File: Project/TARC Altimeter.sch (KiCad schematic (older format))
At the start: 19 parts, among them J1 Power Switch, J2 Programmer Breakout (Conn_01x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, J3 CS Switch, Q1 Q_NMOS_GSD, U1 A23_Socket, U2 ATtiny85-20SU, U3 AP2210-3.3, U4 BMP280

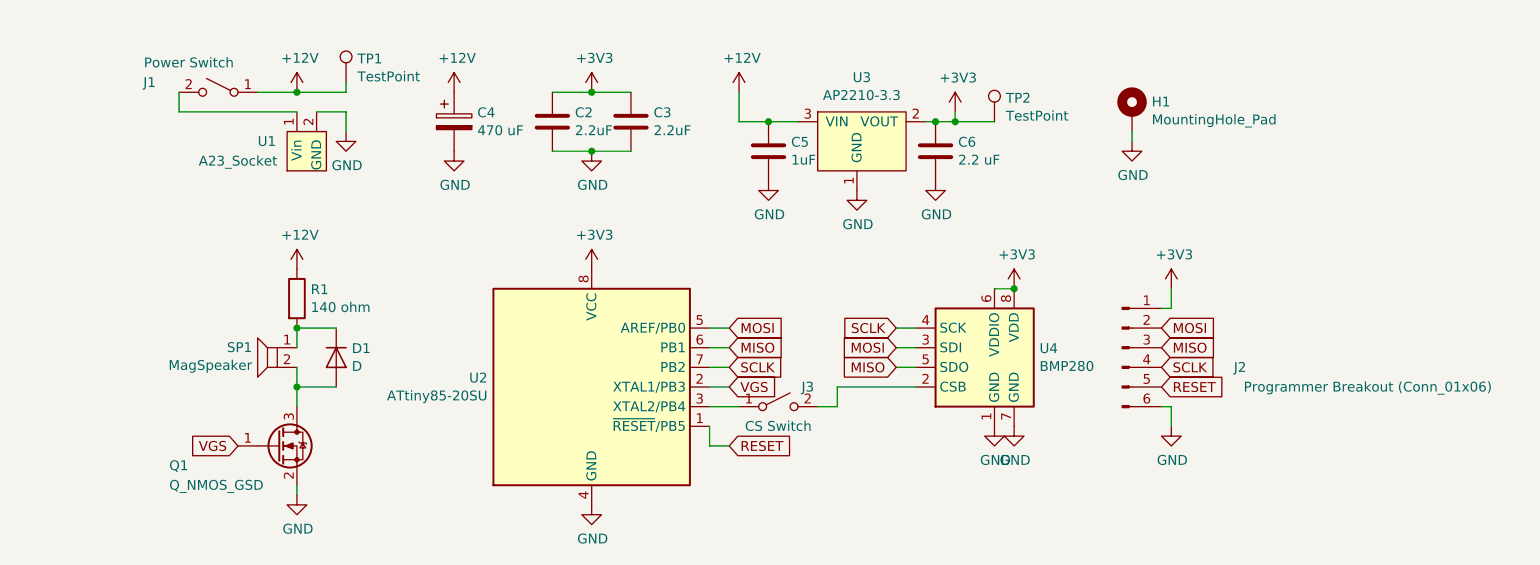
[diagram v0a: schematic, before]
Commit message: added i2c pullups and rearranged components, finalized BMP280 test script
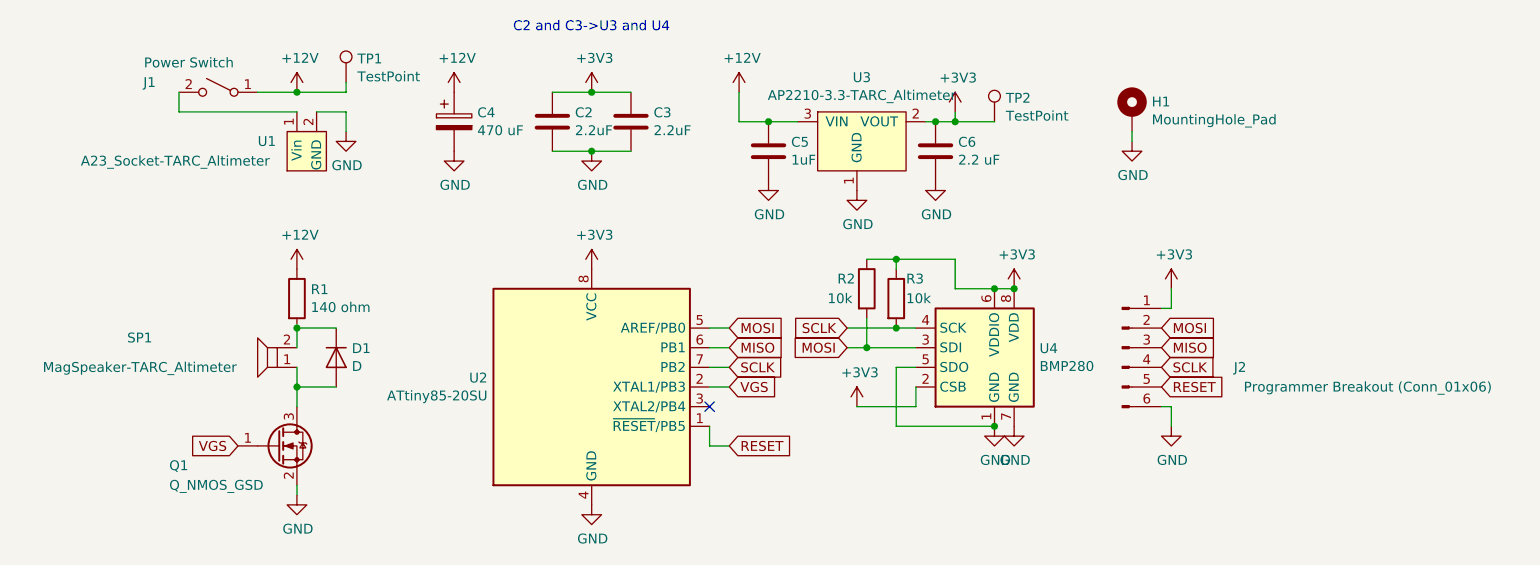
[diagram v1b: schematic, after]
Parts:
- removed J3: CS Switch, Connector_PinHeader_1.27mm:PinHeader_1x02_P1.27mm_Vertical, symbol Switch:SW_SPST
- removed SP1: MagSpeaker, TARC Altimeter:WT-1205, symbol TARC_Altimeter:MagSpeaker
- removed U1: A23_Socket, TARC Altimeter:A23_Socket, symbol TARC_Altimeter:A23_Socket
- removed U3: AP2210-3.3, Package_TO_SOT_SMD:SOT-23, symbol TARC_Altimeter:AP2210-3.3
- added R2, R3: 10k, Resistor_SMD:R_0805_2012Metric_Pad1.15x1.40mm_HandSolder, symbol Device:R
- added SP1: MagSpeaker-TARC_Altimeter, TARC_Altimeter:WT-1205, symbol TARC-Altimeter-rescue:MagSpeaker-TARC_Altimeter
- added U1: A23_Socket-TARC_Altimeter, TARC_Altimeter:A23_Socket, symbol TARC-Altimeter-rescue:A23_Socket-TARC_Altimeter
- added U3: AP2210-3.3-TARC_Altimeter, Package_TO_SOT_SMD:SOT-23, symbol TARC-Altimeter-rescue:AP2210-3.3-TARC_Altimeter
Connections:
- net +12V: now also U3.3 (VIN)
- net +3V3: now also U4.2 (CSB), R2.1, R3.1, U3.2 (VOUT)
- net GND: now also U4.5 (SDO), U1.2 (GND), U3.1 (GND)
- net MISO: no longer U4.5 (SDO)
- net MOSI: now also R2.2
- net SCLK: now also R3.2
- net at D1.1 (K), R1.2: now also SP1.2
- net at D1.2 (A), Q1.3 (D): now also SP1.1
- net at J1.2 (B): now also U1.1 (Vin)
- no-connect marks 0 -> 1
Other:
- note added: "C2 and C3->U3 and U4"
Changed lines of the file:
@@
 EESchema Schematic File Version 4
-LIBS:TARC Altimeter-cache
-EELAYER 26 0
+EELAYER 30 0
 EELAYER END
 $Descr A4 11693 8268
@@
 	1    0    0    -1
 $EndComp
-$Comp
-L TARC_Altimeter:MagSpeaker SP1
-U 1 1 5CB29159
-P 3450 5350
-F 0 "SP1" H 3178 5551 50  0000 L CNN
-F 1 "MagSpeaker" H 3178 5460 50  0000 L CNN
-F 2 "TARC Altimeter:WT-1205" H 3250 5500 50  0001 C CNN
-F 3 "" H 3250 5500 50  0001 C CNN
-	1    3450 5350
-	-1   0    0    -1
-$EndComp
 Wire Wire Line
 	3950 5150 3950 5050
@@
 $EndComp
 $Comp
-L TARC_Altimeter:AP2210-3.3 U3
-U 1 1 5CB5BA2E
-P 6800 4500
-F 0 "U3" H 6825 5225 50  0000 C CNN
-F 1 "AP2210-3.3" H 6825 5134 50  0000 C CNN
-F 2 "Package_TO_SOT_SMD:SOT-23" H 6800 5200 50  0001 C CNN
-F 3 "" H 6800 5200 50  0001 C CNN
-	1    6800 4500
-	1    0    0    -1
-$EndComp
-$Comp
-L power:GND #PWR0107
-U 1 1 5CB5C4BA
-P 6800 4350
-F 0 "#PWR0107" H 6800 4100 50  0001 C CNN
-F 1 "GND" H 6805 4177 50  0000 C CNN
-F 2 "" H 6800 4350 50  0001 C CNN
-F 3 "" H 6800 4350 50  0001 C CNN
-	1    6800 4350
-	1    0    0    -1
-$EndComp
-$Comp
 L power:+3V3 #PWR0108
 U 1 1 5CB5D138
@@
 Wire Wire Line
 	7100 5250 7000 5250
-Wire Wire Line
-	7100 5150 7000 5150
-Text GLabel 7000 5150 0    50   Input ~ 0
-MOSI
-Wire Wire Line
-	7100 5050 7000 5050
 $Comp
 L Device:Q_NMOS_GSD Q1
@@
 VGS
 $Comp
-L TARC_Altimeter:A23_Socket U1
-U 1 1 5CB93965
-P 4000 4150
-F 0 "U1" H 3750 4200 50  0000 L CNN
-F 1 "A23_Socket" H 3450 4100 50  0000 L CNN
-F 2 "TARC Altimeter:A23_Socket" H 4000 4050 50  0001 C CNN
-F 3 "" H 4000 4050 50  0001 C CNN
-	1    4000 4150
-	1    0    0    -1
-$EndComp
-$Comp
 L power:+12V #PWR0111
 U 1 1 5CB94018
@@
 Text GLabel 6150 5050 2    50   Input ~ 0
 MOSI
-Text GLabel 7000 5250 0    50   Input ~ 0
-MISO
 Wire Wire Line
 	6050 5050 6150 5050
@@
 	1    0    0    -1
 $EndComp
-Text GLabel 7000 5050 0    50   Input ~ 0
-SCLK
 Text GLabel 6150 5150 2    50   Input ~ 0
 MISO
@@
 Wire Wire Line
 	3350 3850 3350 3950
-$Comp
-L Switch:SW_SPST J3
-U 1 1 5D45E1A8
-P 6400 5450
-F 0 "J3" H 6550 5550 50  0000 C CNN
-F 1 "CS Switch" H 6400 5350 50  0000 C CNN
-F 2 "Connector_PinHeader_1.27mm:PinHeader_1x02_P1.27mm_Vertical" H 6400 5450 50  0001 C CNN
-F 3 "~" H 6400 5450 50  0001 C CNN
-	1    6400 5450
-	1    0    0    -1
-$EndComp
-Wire Wire Line
-	6050 5450 6200 5450
-Wire Wire Line
-	6700 5350 7100 5350
-Wire Wire Line
-	6700 5350 6700 5450
-Wire Wire Line
-	6700 5450 6600 5450
 Wire Wire Line
 	6050 5550 6050 5650
@@
 Wire Wire Line
 	8200 4050 8200 4100
+$Comp
+L power:GND #PWR0107
+U 1 1 5CB5C4BA
+P 6800 4350
+F 0 "#PWR0107" H 6800 4100 50  0001 C CNN
+F 1 "GND" H 6805 4177 50  0000 C CNN
+F 2 "" H 6800 4350 50  0001 C CNN
+F 3 "" H 6800 4350 50  0001 C CNN
+	1    6800 4350
+	1    0    0    -1
+$EndComp
+Wire Wire Line
+	7000 5250 7000 5550
+Wire Wire Line
+	7000 5550 7500 5550
+Connection ~ 7500 5550
+$Comp
+L TARC-Altimeter-rescue:A23_Socket-TARC_Altimeter U1
+U 1 1 5FED539E
+P 4000 4150
+F 0 "U1" H 3750 4200 50  0000 L CNN
+F 1 "A23_Socket-TARC_Altimeter" H 2850 4100 50  0000 L CNN
+F 2 "TARC_Altimeter:A23_Socket" H 4000 4050 50  0001 C CNN
+F 3 "" H 4000 4050 50  0001 C CNN
+	1    4000 4150
+	1    0    0    -1
+$EndComp
+$Comp
+L TARC-Altimeter-rescue:MagSpeaker-TARC_Altimeter SP1
+U 1 1 5FED5B84
+P 3450 5050
+F 0 "SP1" H 3750 5100 50  0000 C CNN
+F 1 "MagSpeaker-TARC_Altimeter" H 3750 5250 50  0000 C CNN
+F 2 "TARC_Altimeter:WT-1205" H 3250 5200 50  0001 C CNN
+F 3 "" H 3250 5200 50  0001 C CNN
+	1    3450 5050
+	-1   0    0    1
+$EndComp
+NoConn ~ 6050 5450
+$Comp
+L Device:R R3
+U 1 1 5FEE4847
+P 7000 4900
+F 0 "R3" H 7050 5000 50  0000 L CNN
+F 1 "10k" H 7050 4900 50  0000 L CNN
+F 2 "Resistor_SMD:R_0805_2012Metric_Pad1.15x1.40mm_HandSolder" V 6930 4900 50  0001 C CNN
+F 3 "~" H 7000 4900 50  0001 C CNN
+	1    7000 4900
+	1    0    0    -1
+$EndComp
+$Comp
+L Device:R R2
+U 1 1 5FEE3DD7
+P 6850 4850
+F 0 "R2" H 6700 4900 50  0000 L CNN
+F 1 "10k" H 6650 4800 50  0000 L CNN
+F 2 "Resistor_SMD:R_0805_2012Metric_Pad1.15x1.40mm_HandSolder" V 6780 4850 50  0001 C CNN
+F 3 "~" H 6850 4850 50  0001 C CNN
+	1    6850 4850
+	1    0    0    -1
+$EndComp
+Connection ~ 7000 5050
+Wire Wire Line
+	6750 5050 7000 5050
+Wire Wire Line
+	6750 5150 6850 5150
+Wire Wire Line
+	6850 5000 6850 5150
+Connection ~ 6850 5150
+Wire Wire Line
+	7000 4700 7000 4750
+Wire Wire Line
+	7300 4700 7300 4850
+Connection ~ 7000 4700
+Connection ~ 7500 4850
+Wire Wire Line
+	7300 4850 7500 4850
+Wire Wire Line
+	6850 4700 7000 4700
+Text GLabel 6750 5150 0    50   Input ~ 0
+MOSI
+Text GLabel 6750 5050 0    50   Input ~ 0
+SCLK
+Wire Wire Line
+	7000 5050 7100 5050
+Wire Wire Line
+	6850 5150 7100 5150
+Wire Wire Line
+	7000 4700 7300 4700
+$Comp
+L power:+3V3 #PWR0122
+U 1 1 5FEFA896
+P 6800 5450
+F 0 "#PWR0122" H 6800 5300 50  0001 C CNN
+F 1 "+3V3" H 6815 5623 50  0000 C CNN
+F 2 "" H 6800 5450 50  0001 C CNN
+F 3 "" H 6800 5450 50  0001 C CNN
+	1    6800 5450
+	1    0    0    -1
+$EndComp
+Wire Wire Line
+	6800 5450 7100 5450
+Wire Wire Line
+	7100 5450 7100 5350
+Text Notes 5050 3550 0    50   ~ 0
+C2 and C3->U3 and U4
+$Comp
+L TARC-Altimeter-rescue:AP2210-3.3-TARC_Altimeter U3
+U 1 1 5FED6C3E
+P 6800 4500
+F 0 "U3" H 6825 5225 50  0000 C CNN
+F 1 "AP2210-3.3-TARC_Altimeter" H 6825 5134 50  0000 C CNN
+F 2 "Package_TO_SOT_SMD:SOT-23" H 6800 5200 50  0001 C CNN
+F 3 "" H 6800 5200 50  0001 C CNN
+	1    6800 4500
+	1    0    0    -1
+$EndComp
 $EndSCHEMATC

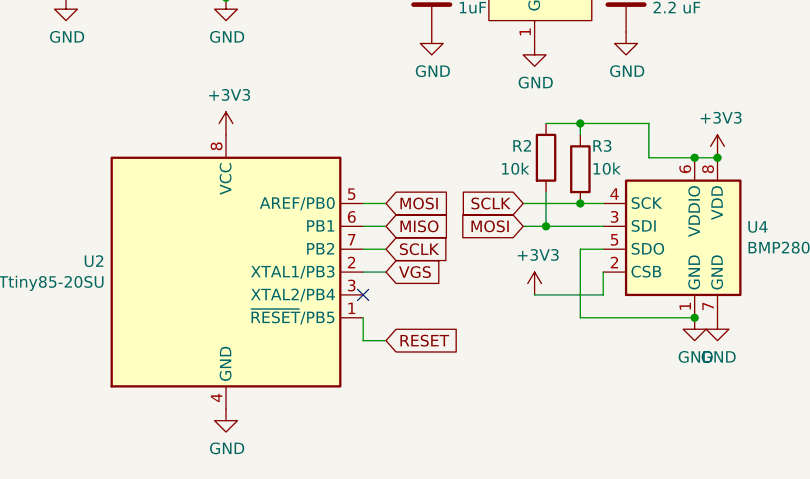
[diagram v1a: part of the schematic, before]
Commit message: changed VGS pin
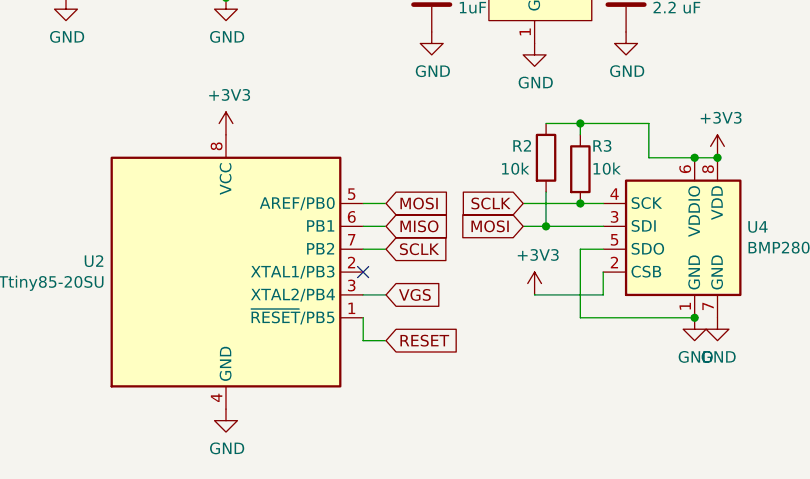
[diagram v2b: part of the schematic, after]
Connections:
- net VGS: now also U2.3 (XTAL2/PB4); no longer U2.2 (XTAL1/PB3)
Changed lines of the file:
@@
-$EndComp
-$Comp
-L MCU_Microchip_ATtiny:ATtiny85-20SU U2
-U 1 1 5CB994CC
-P 5450 5350
-F 0 "U2" H 4920 5396 50  0000 R CNN
-F 1 "ATtiny85-20SU" H 4920 5305 50  0000 R CNN
-F 2 "Package_SO:SOIJ-8_5.3x5.3mm_P1.27mm" H 5450 5350 50  0001 C CIN
-F 3 "http://ww1.microchip.com/downloads/en/DeviceDoc/atmel-2586-avr-8-bit-microcontroller-attiny25-attiny45-attiny85_datasheet.pdf" H 5450 5350 50  0001 C CNN
-	1    5450 5350
-	1    0    0    -1
 $EndComp
 $Comp
@@
 	1    0    0    -1
 $EndComp
-Text GLabel 6150 5350 2    50   Input ~ 0
+Text GLabel 6150 5450 2    50   Input ~ 0
 VGS
 Text GLabel 6150 5250 2    50   Input ~ 0
@@
 Wire Wire Line
 	6050 5150 6150 5150
-Wire Wire Line
-	6050 5350 6150 5350
 $Comp
 L power:GND #PWR0116
@@
 	-1   0    0    1
 $EndComp
-NoConn ~ 6050 5450
 $Comp
 L Device:R R3
@@
 	1    0    0    -1
 $EndComp
+$Comp
+L MCU_Microchip_ATtiny:ATtiny85-20SU U2
+U 1 1 5CB994CC
+P 5450 5350
+F 0 "U2" H 4920 5396 50  0000 R CNN
+F 1 "ATtiny85-20SU" H 4920 5305 50  0000 R CNN
+F 2 "Package_SO:SOIJ-8_5.3x5.3mm_P1.27mm" H 5450 5350 50  0001 C CIN
+F 3 "http://ww1.microchip.com/downloads/en/DeviceDoc/atmel-2586-avr-8-bit-microcontroller-attiny25-attiny45-attiny85_datasheet.pdf" H 5450 5350 50  0001 C CNN
+	1    5450 5350
+	1    0    0    -1
+$EndComp
+NoConn ~ 6050 5350
+Wire Wire Line
+	6050 5450 6150 5450
 $EndSCHEMATC
